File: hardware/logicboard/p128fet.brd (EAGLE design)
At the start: 95 x 72 mm, 30 parts, among them IC1 74LS595N, IC2 74LS595N, K1 AQG12105, K10 AQG12105, K11 AQG12105, K12 AQG12105, K13 AQG12105, K14 AQG12105, K15 AQG12105, K16 AQG12105, K2 AQG12105, K3 AQG12105, K4 AQG12105, K5 AQG12105, K6 AQG12105, K7 AQG12105, K8 AQG12105, K9 AQG12105

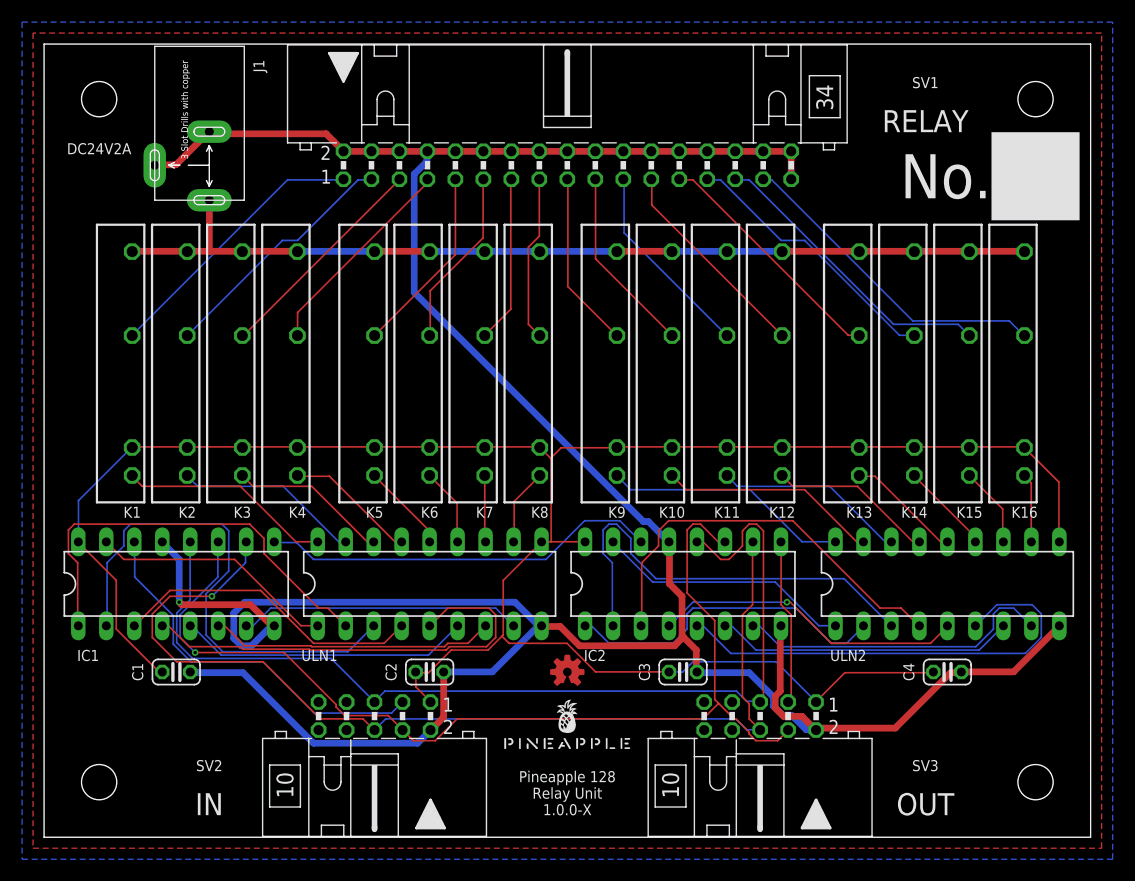
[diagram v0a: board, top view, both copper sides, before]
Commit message: Added FET version.
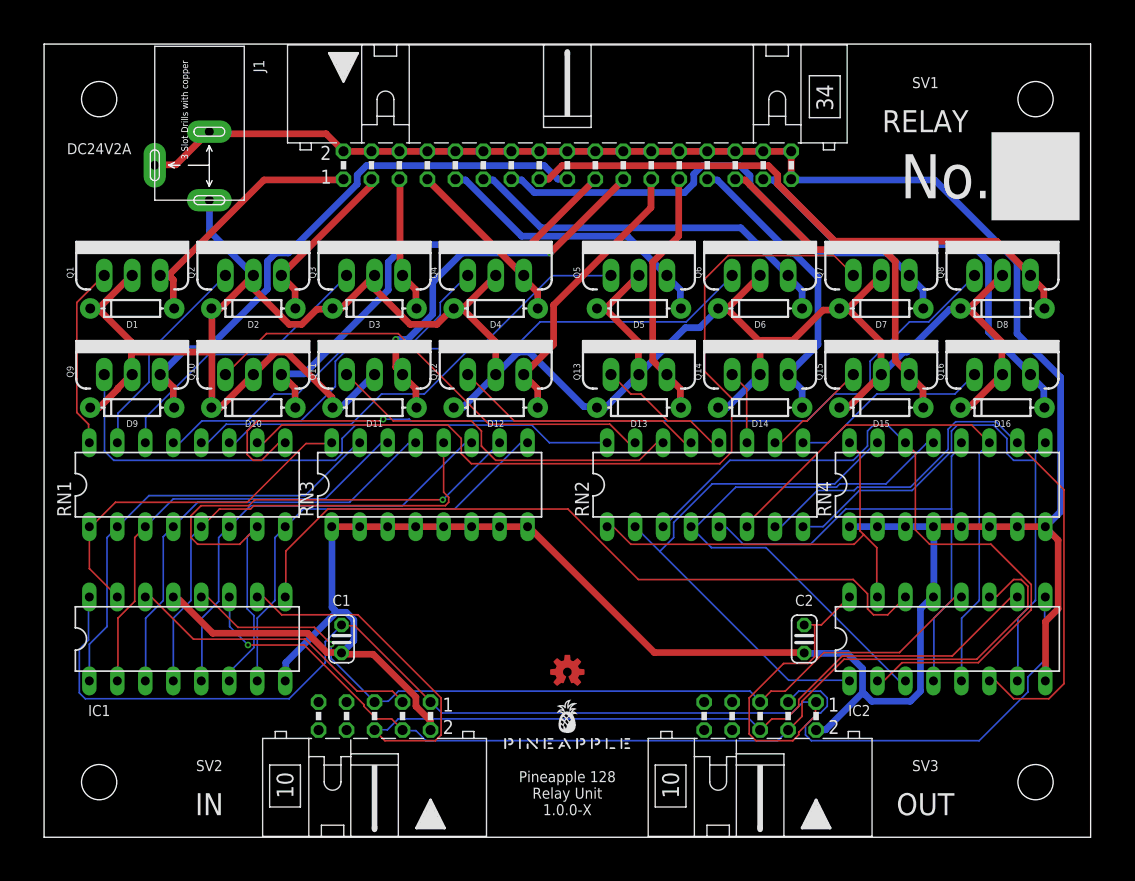
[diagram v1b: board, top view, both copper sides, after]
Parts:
- removed C3, C4: (no value), resistor:C025-024X044
- removed K1, K10, K11, K12, K13, K14, K15, K16, K2, K3, K4, K5, K6, K7, K8, K9: AQG12105, relay:AQG
- removed ULN1, ULN2: (no value), SparkFun-IC-Special-Function:DIL18
- added D1, D10, D11, D12, D13, D14, D15, D16, D2, D3, D4, D5, D6, D7, D8, D9: 200mA/100V/1V, SparkFun-DiscreteSemi:DIODE-1N4148
- added Q1, Q10, Q11, Q12, Q13, Q14, Q15, Q16, Q2, Q3, Q4, Q5, Q6, Q7, Q8, Q9: 60V/32A/35mΩ, SparkFun-DiscreteSemi:TO220V
- added RN1, RN2: 220, resistor-dil:DIL16
- added RN3, RN4: 10k, resistor-dil:DIL16
- moved C2 34.1 mm to (69.0, 18.0), turned to 270 degrees
- moved IC2 24.5 mm to (82.0, 18.0)
- moved C1 15.3 mm to (27.0, 18.0), turned to 270 degrees
- moved IC1 5.10 mm to (13.0, 18.0)
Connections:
- removed net R1: K1.-, ULN1.18
- removed net R10: K10.-, ULN2.17
- removed net R11: K11.-, ULN2.16
- removed net R12: K12.-, ULN2.15
- removed net R13: K13.-, ULN2.14
- removed net R14: K14.-, ULN2.13
- removed net R15: K15.-, ULN2.12
- removed net R16: K16.-, ULN2.11
- removed net R2: K2.-, ULN1.17
- removed net R3: K3.-, ULN1.16
- removed net R4: K4.-, ULN1.15
- removed net R5: K5.-, ULN1.14
- removed net R6: K6.-, ULN1.13
- removed net R7: K7.-, ULN1.12
- removed net R8: K8.-, ULN1.11
- removed net R9: K9.-, ULN2.18
- new net N$1: Q1.1, RN1.16
- new net N$10: Q9.1, RN2.16
- new net N$11: Q10.1, RN2.15
- new net N$12: Q14.1, RN2.11
- new net N$13: Q11.1, RN2.14
- new net N$14: Q15.1, RN2.10
- new net N$15: Q12.1, RN2.13
- new net N$16: Q16.1, RN2.9
- new net N$2: Q2.1, RN1.15
- new net N$25: Q13.1, RN2.12
- new net N$3: Q3.1, RN1.14
- new net N$4: Q4.1, RN1.13
- new net N$5: Q5.1, RN1.12
- new net N$6: Q6.1, RN1.11
- new net N$7: Q7.1, RN1.10
- new net N$8: Q8.1, RN1.9
- net +24V: now also D1.C, D10.C, D11.C, D12.C, D13.C, D14.C, D15.C, D16.C, D2.C, D3.C, D4.C, D5.C, D6.C, D7.C, D8.C, D9.C, Q1.2, Q10.2, Q11.2, Q12.2, Q13.2, Q14.2, Q15.2, Q16.2, Q2.2, Q3.2, Q4.2, Q5.2, Q6.2, Q7.2, Q8.2, Q9.2; no longer K1.O2, K10.O2, K11.O2, K12.O2, K13.O2, K14.O2, K15.O2, K16.O2, K2.O2, K3.O2, K4.O2, K5.O2, K6.O2, K7.O2, K8.O2, K9.O2
- net GND: now also RN3.1, RN3.2, RN3.3, RN3.4, RN3.5, RN3.6, RN3.7, RN3.8, RN4.1, RN4.2, RN4.3, RN4.4, RN4.5, RN4.6, RN4.7, RN4.8; no longer C3.2, C4.2, ULN1.9, ULN2.9
- net S1: now also RN1.1, RN3.16; no longer ULN1.1
- net S10: now also RN2.2, RN4.15; no longer ULN2.2
- net S11: now also RN2.3, RN4.14; no longer ULN2.3
- net S12: now also RN2.4, RN4.13; no longer ULN2.4
- net S13: now also RN2.5, RN4.12; no longer ULN2.5
- net S14: now also RN2.6, RN4.11; no longer ULN2.6
- net S15: now also RN2.7, RN4.10; no longer ULN2.7
- net S16: now also RN2.8, RN4.9; no longer ULN2.8
- net S2: now also RN1.2, RN3.15; no longer ULN1.2
- net S3: now also RN1.3, RN3.14; no longer ULN1.3
- net S4: now also RN1.4, RN3.13; no longer ULN1.4
- net S5: now also RN1.5, RN3.12; no longer ULN1.5
- net S6: now also RN1.6, RN3.11; no longer ULN1.6
- net S7: now also RN1.7, RN3.10; no longer ULN1.7
- net S8: now also RN1.8, RN3.9; no longer ULN1.8
- net S9: now also RN2.1, RN4.16; no longer ULN2.1
- net VCC: no longer C3.1, C4.1, K1.+, K10.+, K11.+, K12.+, K13.+, K14.+, K15.+, K16.+, K2.+, K3.+, K4.+, K5.+, K6.+, K7.+, K8.+, K9.+, ULN1.10, ULN2.10
- net X1: now also D1.A, Q1.3; no longer K1.O1
- net X10: now also D10.A, Q10.3; no longer K10.O1
- net X11: now also D11.A, Q11.3; no longer K11.O1
- net X12: now also D12.A, Q12.3; no longer K12.O1
- net X13: now also D13.A, Q13.3; no longer K13.O1
- net X14: now also D14.A, Q14.3; no longer K14.O1
- net X15: now also D15.A, Q15.3; no longer K15.O1
- net X16: now also D16.A, Q16.3; no longer K16.O1
- net X2: now also D2.A, Q2.3; no longer K2.O1
- net X3: now also D3.A, Q3.3; no longer K3.O1
- net X4: now also D4.A, Q4.3; no longer K4.O1
- net X5: now also D5.A, Q5.3; no longer K5.O1
- net X6: now also D6.A, Q6.3; no longer K6.O1
- net X7: now also D7.A, Q7.3; no longer K7.O1
- net X8: now also D8.A, Q8.3; no longer K8.O1
- net X9: now also D9.A, Q9.3; no longer K9.O1
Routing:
- net +24V: track 85.9 -> 222.1 mm
- net VCC: track 195.9 -> 111.3 mm
- net N$8: track 0.00 -> 79.7 mm, vias 0 -> 1
- net N$7: track 0.00 -> 78.3 mm
- net N$10: track 0.00 -> 55.7 mm
- net N$6: track 0.00 -> 52.0 mm
- net N$5: track 0.00 -> 44.8 mm
- net N$11: track 0.00 -> 42.8 mm
- net X8: track 15.0 -> 53.3 mm
- net X9: track 16.1 -> 50.9 mm
- net N$4: track 0.00 -> 33.7 mm
- net N$13: track 0.00 -> 33.4 mm
- net S15: track 27.1 -> 59.4 mm
- net N$9: track 36.2 -> 67.5 mm
- net X7: track 15.2 -> 46.3 mm
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- removed copper zone on layer 1, net GND
- removed copper zone on layer 16, net GND
